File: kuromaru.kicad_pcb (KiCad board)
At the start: 2 copper layers, 125.5 x 95.1 mm, 63 parts, among them J1 USB_C_Receptacle_USB2.0, J102 Serial, J5 Conn_01x02, SW1 SW_Push, SW2 SW_Push, U1 RP2040, U2 GD25Q80CEIGR, U3 XC6210B332MR-G, U4 25LCxxx, Y1 Crystal_GND24

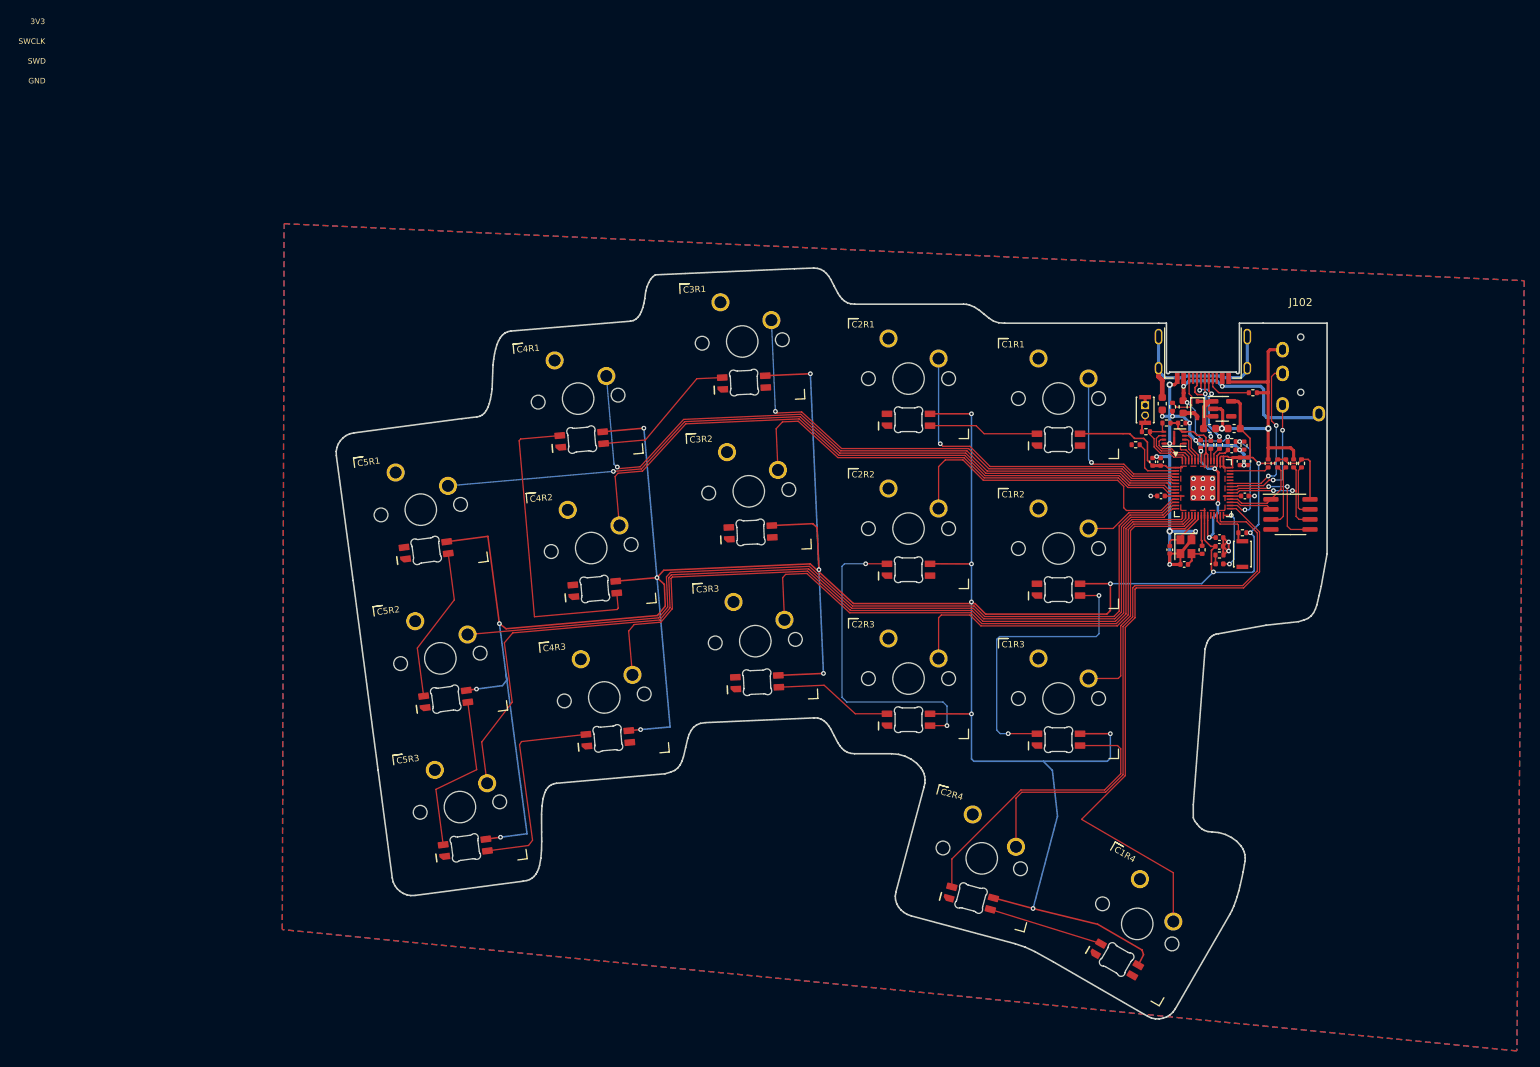
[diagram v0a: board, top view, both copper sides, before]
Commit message: Clean reroute of the thumb cluster
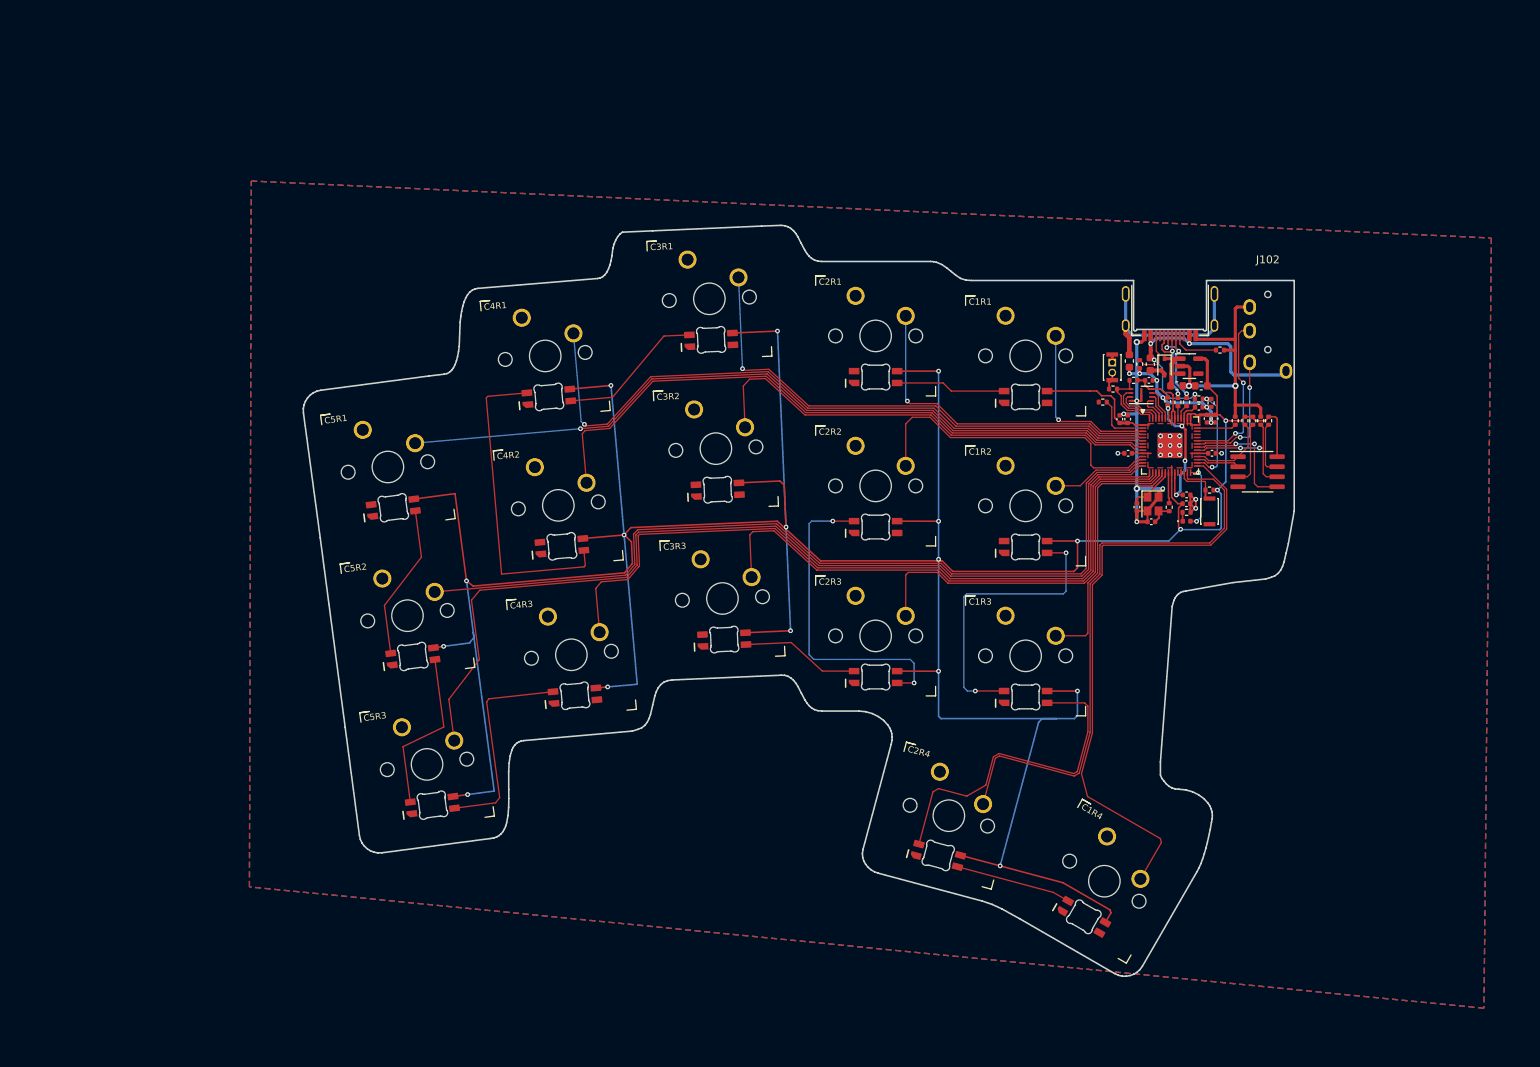
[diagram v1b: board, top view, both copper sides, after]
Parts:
- moved C12 6.82 mm to (138.3, 46.7)
- moved R1 6.82 mm to (145.7, 58.5)
- moved SW1 6.82 mm to (148.6, 58.4)
- moved FB1 6.82 mm to (138.5, 39.3)
- moved C1R3 6.82 mm to (125.3, 76.7)
- moved R14 6.82 mm to (151.9, 46.9)
- moved C8 6.82 mm to (145.7, 56.3)
- moved C3R3 6.82 mm to (86.9, 69.4)
- moved C5R3 6.82 mm to (49.5, 90.4)
- moved U2 6.82 mm to (140.0, 43.6)
- moved C1 6.82 mm to (144.5, 42.5)
- moved C1R4 6.82 mm to (135.3, 105.2)
- moved R2 6.82 mm to (148.6, 55.7)
- moved C4 6.82 mm to (141.3, 59.7)
- moved C15 6.82 mm to (137.3, 46.7)
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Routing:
- net Net-(C1R3-Pad2): track 37.9 -> 42.8 mm
- net switch_c1r4: track 78.3 -> 75.7 mm
- net +3V3: track 495.8 -> 497.4 mm
- net switch_c2r4: track 72.7 -> 74.2 mm
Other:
- board text removed: "3V3"
- board text removed: "GND"
- board text removed: "SWCLK"
- board text removed: "SWD"

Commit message: More route cleanup
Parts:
- moved R15 2.20 mm to (135.2, 46.7)
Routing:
- net Net-(C5R1-Pad4): track 0.00 -> 109.6 mm
- net rgb_din: track 7.28 -> 5.43 mm
- net switch_c4r3: track 95.6 -> 94.9 mm
- net switch_c5r2: track 109.4 -> 108.6 mm
- net switch_c5r3: track 124.4 -> 123.7 mm
- net Net-(C4R2-Pad2): track 40.3 -> 40.8 mm, vias 0 -> 2
- net switch_c5r1: vias 1 -> 0

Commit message: Fix serial connector
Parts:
- moved J102 1.85 mm to (155.7, 32.5)
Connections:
- J102 pad R1: serial_tx -> serial_rx
- J102 pad R2: serial_rx -> serial_tx
- J102 pad S: GND -> VBUS
- J102 pad T: VBUS -> GND
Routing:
- net VBUS: track 35.2 -> 26.8 mm
- net GND: track 112.5 -> 117.5 mm
- net serial_rx: track 20.5 -> 24.9 mm, vias 2 -> 1
- net serial_tx: track 16.4 -> 20.6 mm, vias 2 -> 1

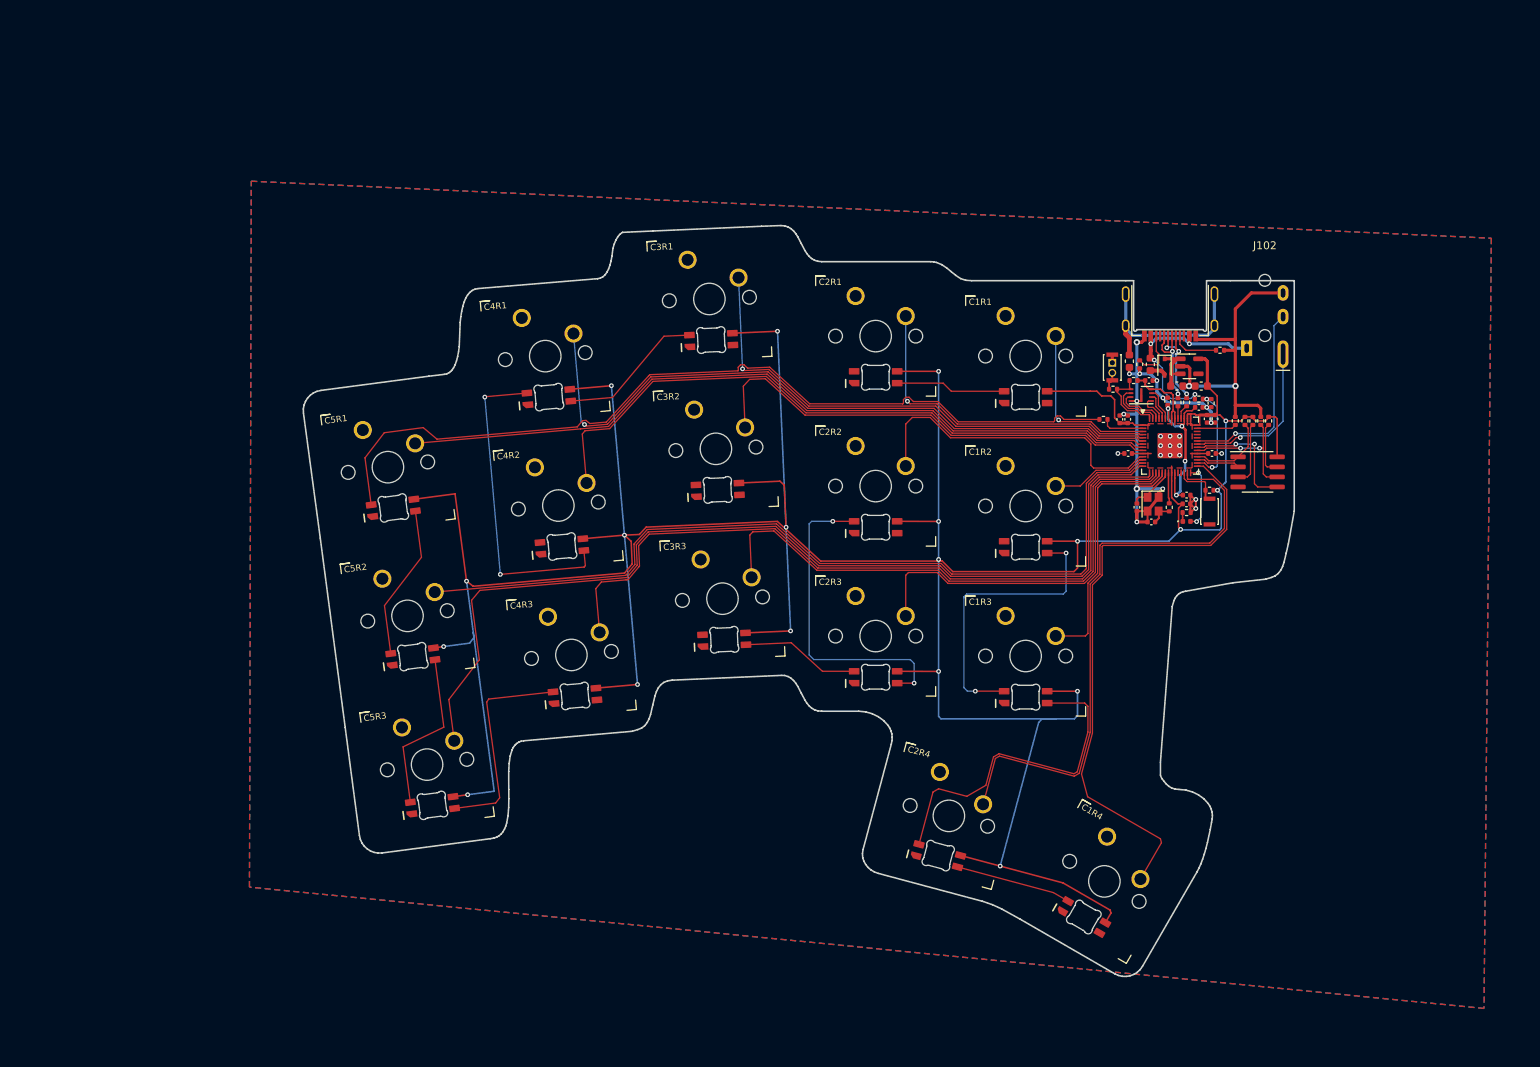
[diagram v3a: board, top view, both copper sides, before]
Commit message: Make thumb 1.5u
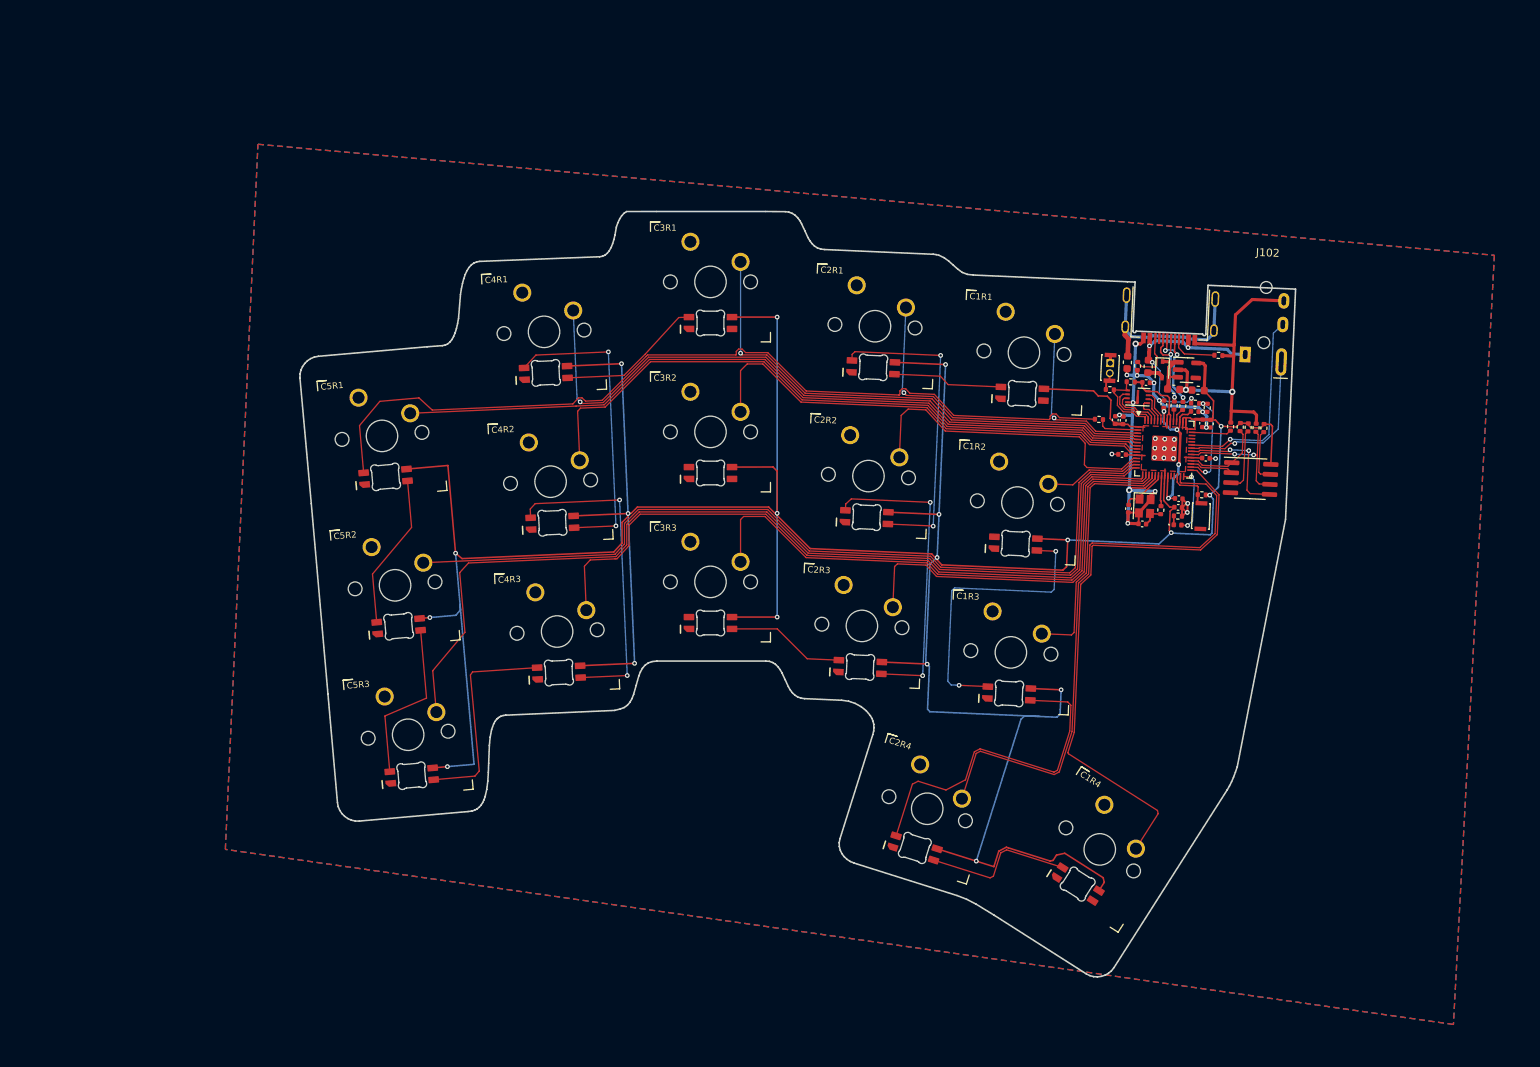
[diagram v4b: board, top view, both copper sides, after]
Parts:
- moved C5R3 4.48 mm to (47.1, 86.7), turned to 5 degrees
- moved C5R2 4.18 mm to (45.5, 67.7), turned to 5 degrees
- moved C1R4 4.10 mm to (134.7, 101.2), turned to -32.5 degrees
- moved C5R1 4.03 mm to (43.8, 48.8), turned to 5 degrees
- moved C4R3 3.48 mm to (66.0, 73.6), turned to 2.5 degrees
- moved C4R2 3.18 mm to (65.2, 54.6), turned to 2.5 degrees
- moved C4R1 3.08 mm to (64.3, 35.6), turned to 2.5 degrees
- moved C2R4 2.89 mm to (112.9, 96.0), turned to -17.5 degrees
- moved C3R3 2.61 mm to (85.4, 67.3), turned to 0 degrees
- moved C3R2 2.25 mm to (85.4, 48.3), turned to 0 degrees
- moved C3R1 2.17 mm to (85.4, 29.3), turned to 0 degrees
- moved C2R3 2.17 mm to (104.6, 72.9), turned to -2.5 degrees
- moved C1R3 1.93 mm to (123.5, 76.2), turned to -2.5 degrees
- moved C2R2 1.56 mm to (105.4, 53.9), turned to -2.5 degrees
- moved C2R1 1.25 mm to (106.3, 34.9), turned to -2.5 degrees
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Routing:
- net Net-(C4R2-Pad4): track 0.00 -> 40.9 mm, vias 0 -> 2
- net Net-(C2R1-Pad4): track 0.00 -> 39.5 mm, vias 0 -> 2
- net +3V3: track 497.1 -> 507.6 mm
- net Net-(C1R4-Pad4): track 14.7 -> 19.4 mm
- net switch_c1r4: track 75.7 -> 72.7 mm
- net Net-(C4R1-Pad4): track 40.8 -> 38.8 mm
- net Net-(C2R2-Pad4): track 40.8 -> 39.0 mm
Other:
- board size 125.5 x 95.1 mm -> 126.1 x 97 mm

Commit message: Remove RGB
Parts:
- removed C15: 1µ, Capacitor_SMD:C_0402_1005Metric
- removed R15: 300, Resistor_SMD:R_0402_1005Metric
- C1R1, C1R2, C1R3, C1R4, C2R1, C2R2, C2R3, C2R4, C3R1, C3R2, C3R3, C4R1, C4R2, C4R3, C5R1, C5R2, C5R3: footprint local-libraries:delay_SW_MX_RGB -> local-libraries:delay_SW_MX_flipped
- moved C5R1 2.91 mm to (43.1, 51.6), turned to 7.5 degrees
- moved C5R3 2.78 mm to (48.0, 89.3), turned to 7.5 degrees
- moved C5R2 2.72 mm to (45.5, 70.5), turned to 7.5 degrees
- moved J102 2.55 mm to (154.2, 31.4), turned to 0 degrees
- moved C4R1 2.35 mm to (63.0, 37.6), turned to 5 degrees
- moved J1 2.29 mm to (142.1, 27.6), turned to 180 degrees
- moved R16 2.24 mm to (154.6, 45.8), turned to 90 degrees
- moved R4 2.21 mm to (148.5, 36.8), turned to 180 degrees
- moved R13 2.20 mm to (153.6, 45.8), turned to -90 degrees
- moved R17 2.17 mm to (152.6, 45.8), turned to 90 degrees
- moved R12 2.13 mm to (151.6, 45.8), turned to 90 degrees
- moved U4 2.08 mm to (153.2, 52.2), turned to 0 degrees
- moved R14 2.08 mm to (150.4, 45.8), turned to 90 degrees
- moved U3 2.02 mm to (144.6, 38.8), turned to 0 degrees
- moved C2 2.01 mm to (146.1, 41.3), turned to 180 degrees
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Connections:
- C1R1 pad 1: +3V3 -> GND
- C1R1 pad 2: Net-(C1R1-Pad2) -> switch_c1r1
- C1R2 pad 1: +3V3 -> GND
- C1R2 pad 2: Net-(C1R2-Pad2) -> switch_c1r2
- C1R3 pad 1: +3V3 -> GND
- C1R3 pad 2: Net-(C1R3-Pad2) -> switch_c1r3
- C1R4 pad 1: +3V3 -> GND
- C1R4 pad 2: unconnected-(C1R4-Pad2) -> switch_c1r4
- C2R1 pad 1: +3V3 -> GND
- C2R1 pad 2: Net-(C1R1-Pad4) -> switch_c2r1
- C2R2 pad 1: +3V3 -> GND
- C2R2 pad 2: Net-(C2R1-Pad4) -> switch_c2r2
- C2R3 pad 1: +3V3 -> GND
- C2R3 pad 2: Net-(C2R2-Pad4) -> switch_c2r3
- C2R4 pad 1: +3V3 -> GND
- C2R4 pad 2: Net-(C1R4-Pad4) -> switch_c2r4
- C3R1 pad 1: +3V3 -> GND
- C3R1 pad 2: Net-(C3R1-Pad2) -> switch_c3r1
- C3R2 pad 1: +3V3 -> GND
- C3R2 pad 2: Net-(C3R2-Pad2) -> switch_c3r2
- C3R3 pad 1: +3V3 -> GND
- C3R3 pad 2: Net-(C2R3-Pad4) -> switch_c3r3
- C4R1 pad 1: +3V3 -> GND
- C4R1 pad 2: Net-(C3R1-Pad4) -> switch_c4r1
- C4R2 pad 1: +3V3 -> GND
- C4R2 pad 2: Net-(C4R1-Pad4) -> switch_c4r2
- C4R3 pad 1: +3V3 -> GND
- C4R3 pad 2: Net-(C4R2-Pad4) -> switch_c4r3
- C5R1 pad 1: +3V3 -> GND
- C5R1 pad 2: Net-(C5R1-Pad2) -> switch_c5r1
- C5R2 pad 1: +3V3 -> GND
- C5R2 pad 2: Net-(C5R2-Pad2) -> switch_c5r2
- C5R3 pad 1: +3V3 -> GND
- C5R3 pad 2: Net-(C4R3-Pad4) -> switch_c5r3
- U1 pad 11: switch_c2r2 -> switch_c1r2
- U1 pad 12: switch_c1r2 -> switch_c5r2
- U1 pad 13: switch_c5r2 -> switch_c5r3
- U1 pad 14: switch_c5r3 -> switch_c4r3
- U1 pad 15: switch_c4r3 -> switch_c3r3
- U1 pad 16: switch_c3r3 -> switch_c2r3
- U1 pad 17: switch_c2r3 -> switch_c1r3
- U1 pad 18: switch_c1r3 -> /GPIO15
- U1 pad 2: rgb_din -> switch_c1r1
- U1 pad 3: switch_c1r1 -> switch_c2r1
- U1 pad 4: switch_c2r1 -> switch_c3r1
- U1 pad 5: switch_c3r1 -> switch_c4r1
- U1 pad 6: switch_c4r1 -> switch_c5r1
- U1 pad 7: switch_c5r1 -> switch_c4r2
- U1 pad 8: switch_c4r2 -> switch_c3r2
- U1 pad 9: switch_c3r2 -> switch_c2r2
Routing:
- net +3V3: track 507.6 -> 79.2 mm, vias 19 -> 3
- net Net-(C5R1-Pad4): track 109.6 -> 0.00 mm
- net Net-(C1R3-Pad2): track 42.8 -> 0.00 mm
- net Net-(C4R2-Pad4): track 40.9 -> 0.00 mm, vias 2 -> 0
- net Net-(C2R1-Pad4): track 39.5 -> 0.00 mm, vias 2 -> 0
- net Net-(C2R2-Pad4): track 39.0 -> 0.00 mm, vias 2 -> 0
- net Net-(C4R1-Pad4): track 38.8 -> 0.00 mm, vias 2 -> 0
- net Net-(C1R2-Pad2): track 37.3 -> 0.00 mm, vias 2 -> 0
- net Net-(C4R3-Pad4): track 27.0 -> 0.00 mm
- net Net-(C5R2-Pad2): track 21.4 -> 0.00 mm
- net Net-(C5R1-Pad2): track 19.8 -> 0.00 mm
- net Net-(C1R4-Pad4): track 19.4 -> 0.00 mm
- net Net-(C3R1-Pad4): track 18.5 -> 0.00 mm
- net Net-(C2R3-Pad4): track 15.1 -> 0.00 mm
- net Net-(C1R1-Pad4): track 14.0 -> 0.00 mm
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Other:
- board size 126.1 x 97 mm -> 125.5 x 95.1 mm

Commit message: Ready for order
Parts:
- removed J5: Conn_01x02, Connector_PinHeader_1.27mm:PinHeader_1x02_P1.27mm_Vertical
- removed R12, R13: 100k, Resistor_SMD:R_0402_1005Metric
- removed R16, R17: 5.1k, Resistor_SMD:R_0402_1005Metric
- removed U4: 25LCxxx, Package_SO:SOIC-8_3.9x4.9mm_P1.27mm
- moved SW2 18.3 mm to (136.0, 57.2), turned to 90 degrees
- moved R3 12.8 mm to (136.0, 54.5), turned to 180 degrees
- moved R14 3.22 mm to (147.5, 47.1), turned to 0 degrees
- moved C2 1.25 mm to (147.3, 41.4)
- moved U3 1.15 mm to (145.8, 38.8)
- moved C1 0.85 mm to (143.8, 41.3)
- moved R4 0.71 mm to (148.5, 36.1)
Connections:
- U1 pad 40: /A2 -> hands
- U1 pad 41: hands -> /A3
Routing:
- net /SCLK: track 16.7 -> 0.00 mm, vias 2 -> 0
- net /QSPI_~{CS}: track 9.67 -> 25.4 mm, vias 0 -> 2
- net /MOSI: track 15.5 -> 0.00 mm, vias 2 -> 0
- net +3V3: track 79.2 -> 65.8 mm
- net /EEPROM_CS: track 10.3 -> 0.00 mm
- net GND: track 124.3 -> 134.0 mm, vias 27 -> 26
- net Net-(R17-Pad1): track 8.05 -> 0.00 mm
- net Net-(R16-Pad1): track 6.84 -> 0.00 mm
- net /MISO: track 5.54 -> 0.00 mm
- net hands: track 5.00 -> 1.39 mm
- net serial_rx: track 24.9 -> 22.5 mm, vias 1 -> 0
- net serial_tx: track 20.6 -> 18.4 mm, vias 1 -> 0
- net /VBUS_DET: track 13.0 -> 11.6 mm
- net /LED: track 8.36 -> 9.53 mm
- net switch_c1r4: track 72.7 -> 73.9 mm
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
